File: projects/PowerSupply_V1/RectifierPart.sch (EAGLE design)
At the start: 16 parts, among them X1 OUT, X2 IN

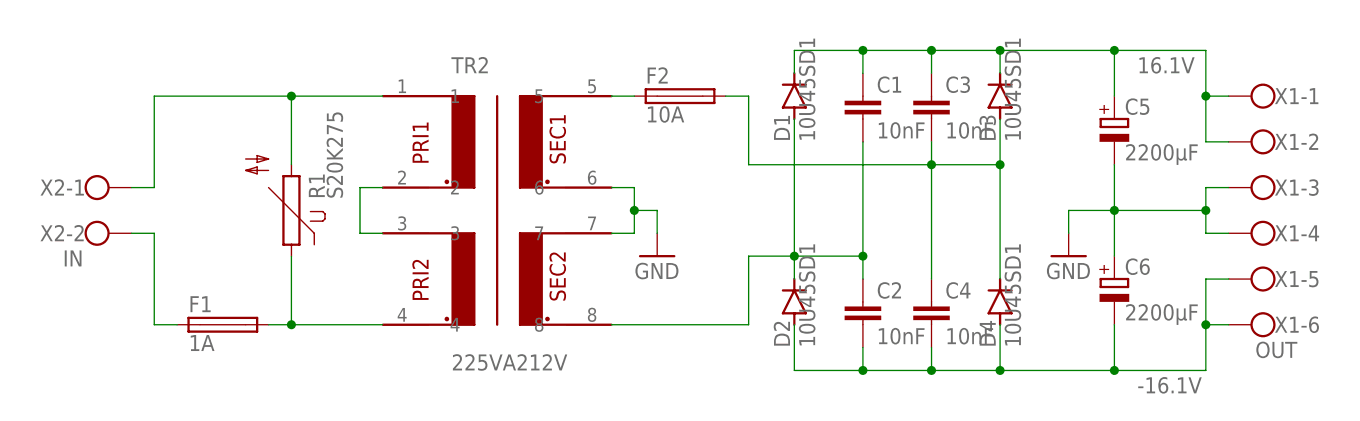
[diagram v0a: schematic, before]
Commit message: feat: power supply
changes:
- version one done
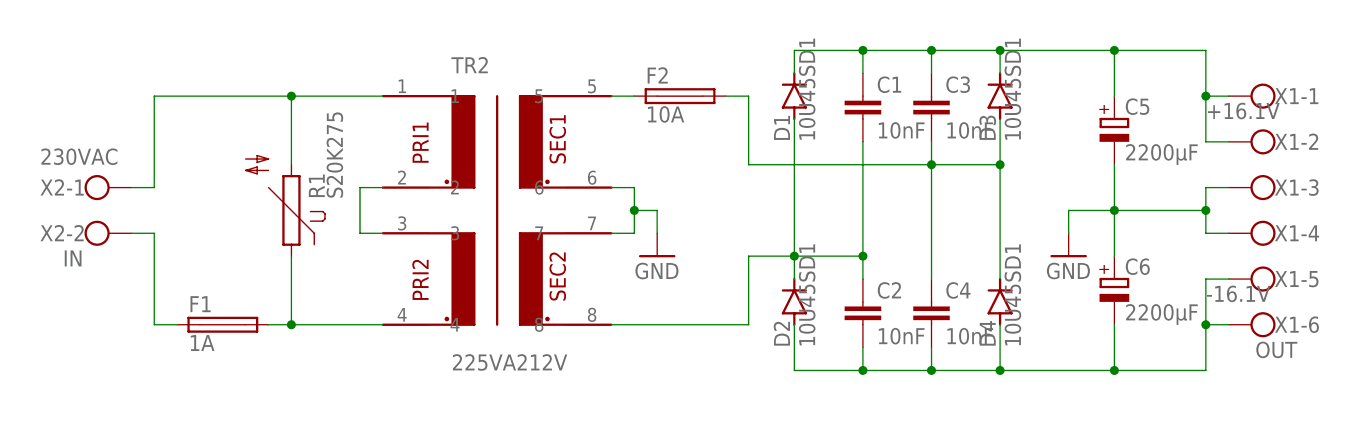
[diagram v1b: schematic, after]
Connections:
- net 16.1V renamed +16.1V
- net N$6 renamed 230VAC
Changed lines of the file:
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@@
 <wire x1="175.26" y1="86.36" x2="175.26" y2="81.28" width="0.1524" layer="91"/>
 <junction x="175.26" y="81.28"/>
-<label x="167.64" y="73.66" size="1.778" layer="95"/>
+<label x="175.26" y="83.82" size="1.778" layer="95"/>
 </segment>
 </net>
-<net name="16.1V" class="0">
+<net name="+16.1V" class="0">
 <segment>
 <pinref part="D1" gate="1" pin="C"/>
@@
 <wire x1="175.26" y1="101.6" x2="175.26" y2="106.68" width="0.1524" layer="91"/>
 <junction x="175.26" y="106.68"/>
-<label x="167.64" y="109.22" size="1.778" layer="95"/>
+<label x="175.26" y="104.14" size="1.778" layer="95"/>
 </segment>
 </net>
@@
 </segment>
 </net>
-<net name="N$6" class="0">
+<net name="230VAC" class="0">
 <segment>
 <pinref part="X2" gate="-1" pin="KL"/>
@@
 <wire x1="83.82" y1="106.68" x2="73.66" y2="106.68" width="0.1524" layer="91"/>
 <junction x="73.66" y="106.68"/>
+<label x="45.72" y="99.06" size="1.778" layer="95"/>
 </segment>
 </net>

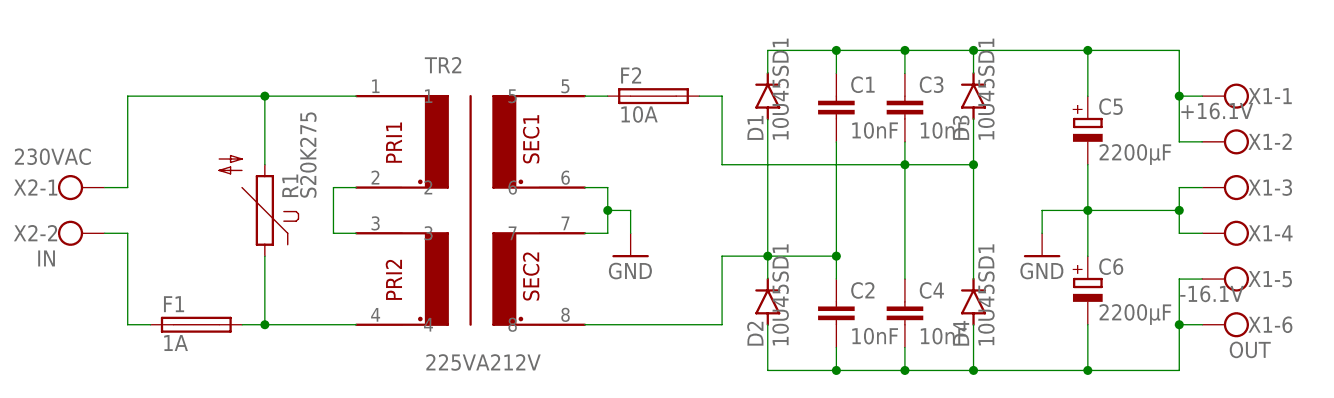
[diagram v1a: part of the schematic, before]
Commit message: feat: power supply
changes:
- small fixes to rectifier capacity
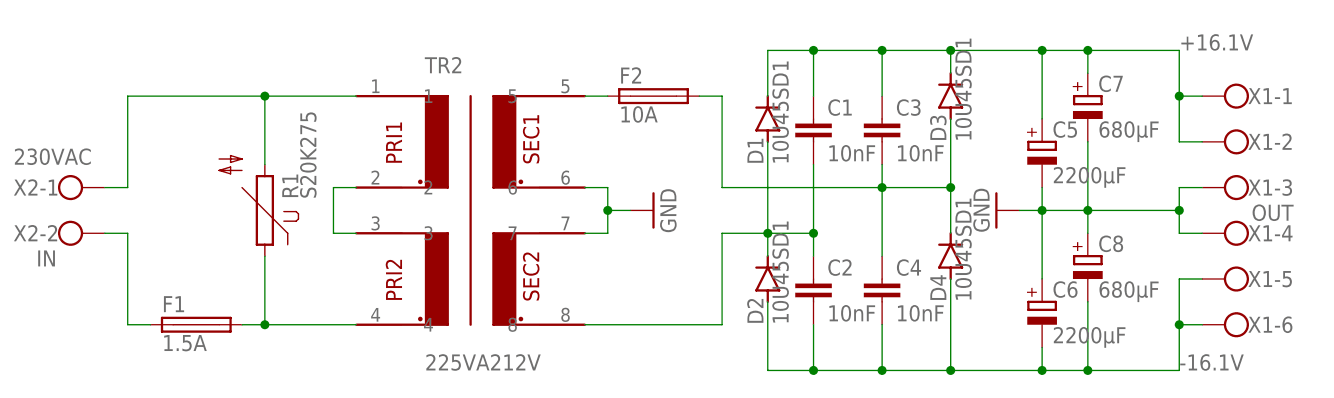
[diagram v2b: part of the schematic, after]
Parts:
- added C7, C8: 680µF, rcl:CPOL-EUE5-13
- F1: value 1A -> 1.5A
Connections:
- net +16.1V: now also C7.+
- net -16.1V: now also C8.-
- net GND: now also C7.-, C8.+
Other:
- moved on the sheet: C1, C2, C3, C4, C5, C6, D1, D2, D3, D4

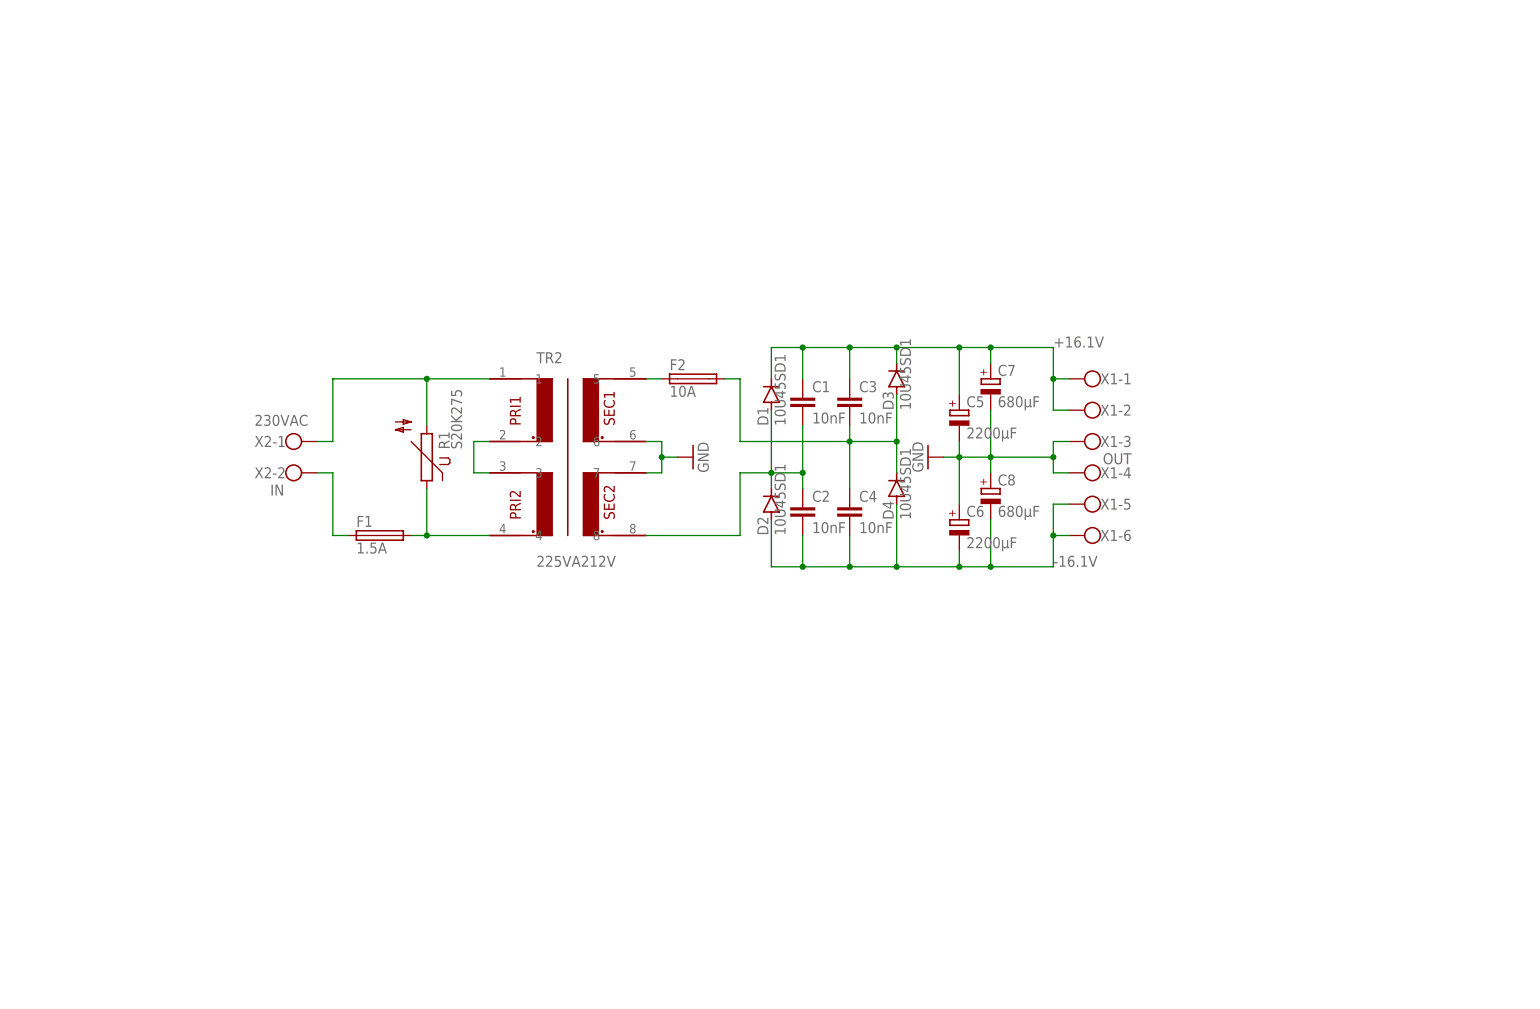
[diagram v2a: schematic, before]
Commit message: feat(rectifier): schematics changed
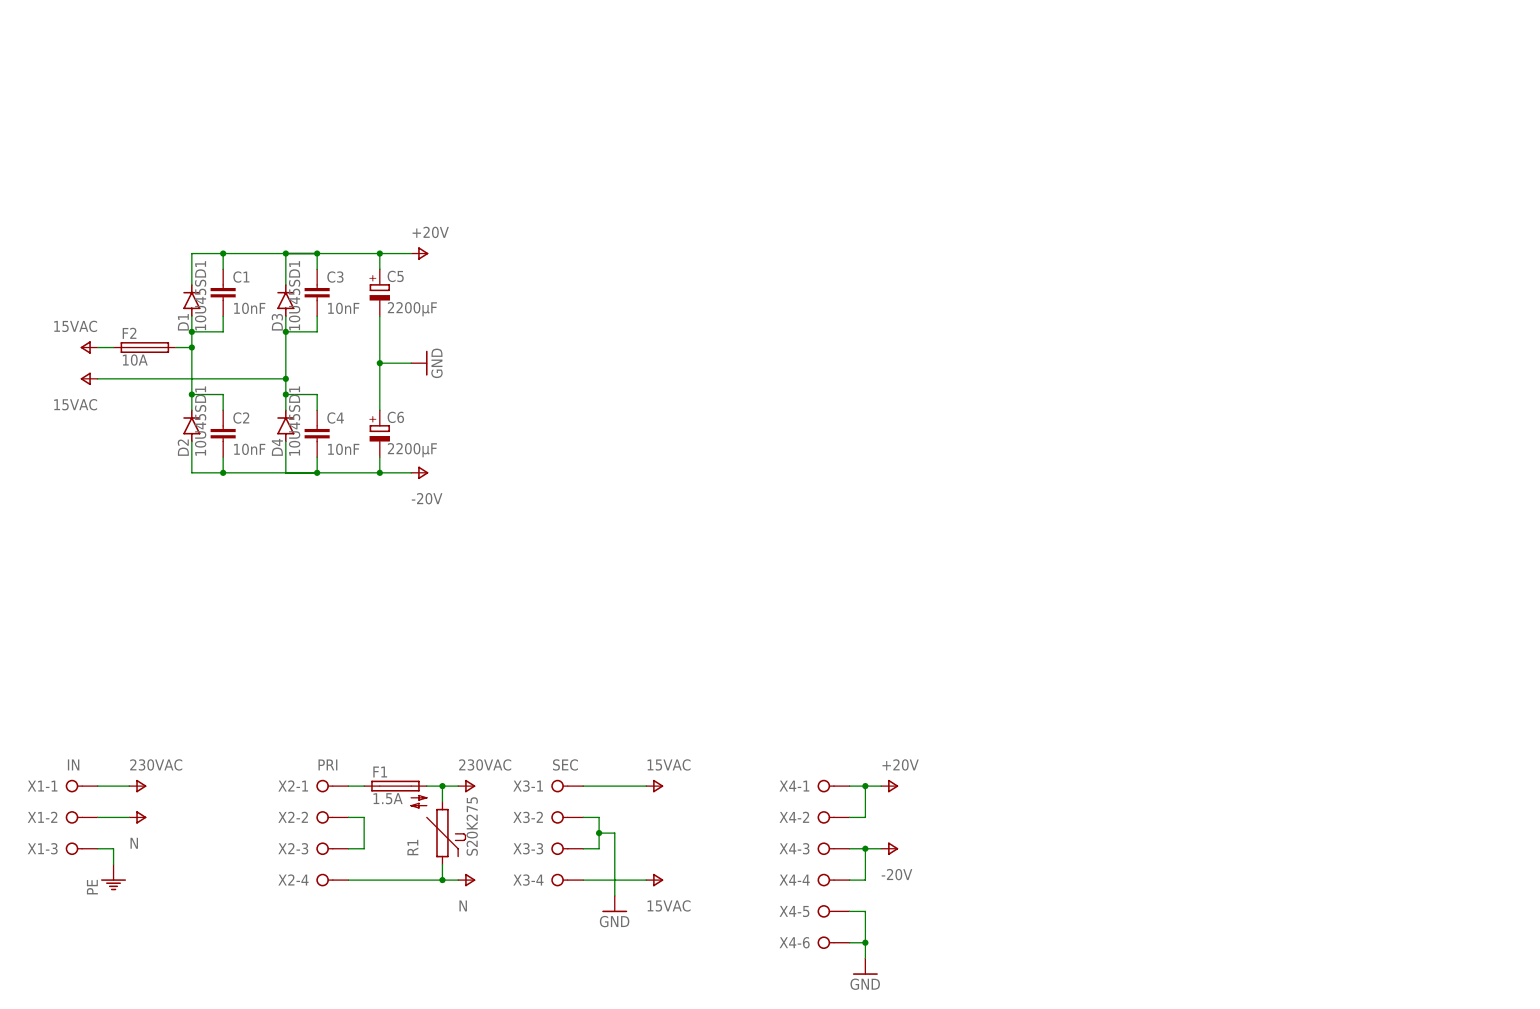
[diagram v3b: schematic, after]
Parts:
- removed C7, C8: 680µF, rcl:CPOL-EUE5-13
- removed TR2: 225VA212V, bb84:225VA212V
- added X3: SEC, con-wago-508:W237-04P
- added X4: (no value), con-wago-508:W237-06P
- X1: value OUT -> IN; device con-wago-500:W237-6 -> con-wago-508:W237-03P
- X2: value IN -> PRI; device con-wago-500:W237-102 -> con-wago-508:W237-04P
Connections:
- removed net +16.1V: C1.1, C3.1, C5.+, C7.+, D1.C, D3.C, X1-1.KL, X1-2.KL
- removed net -16.1V: C2.2, C4.2, C6.-, C8.-, D2.A, D4.A, X1-5.KL, X1-6.KL
- removed net 230VAC: R1.2, TR2.1, X2-1.KL
- removed net N$1: C3.2, C4.1, D3.A, D4.C, F2.2
- removed net N$4: C1.2, C2.1, D1.A, D2.C, TR2.8
- removed net N$7: F1.2, R1.1, TR2.4
- removed net N$8: F1.1, X2-2.KL
- removed net N$9: F2.1, TR2.5
- new net N$2: X2-2.KL, X2-3.KL
- new net N$5: C1.2, C2.1, D1.A, D2.C, F2.2
- new net PE: X1-3.KL
- new net V+: C1.1, C3.1, C5.+, D1.C, D3.C, F1.2, F2.1, R1.2, X1-1.KL, X3-1.KL, X4-1.KL, X4-2.KL
- new net V-: C2.2, C3.2, C4.1, C4.2, C6.-, D2.A, D3.A, D4.A, D4.C, R1.1, X1-2.KL, X2-4.KL, X3-4.KL, X4-3.KL, X4-4.KL
- net GND: now also X3-2.KL, X3-3.KL, X4-5.KL, X4-6.KL; no longer C7.-, C8.+, TR2.6, TR2.7, X1-3.KL, X1-4.KL
- net N$3: now also F1.1, X2-1.KL; no longer TR2.2, TR2.3
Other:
- moved on the sheet: C1, C2, C3, C4, C5, C6, D1, D2, D3, D4, F1, F2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
